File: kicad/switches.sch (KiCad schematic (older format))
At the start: 24 parts, among them SW1 SW_SPDT_MSM, SW2 SW_SPDT_MSM, SW3 SW_SPDT_MSM, SW4 SW_SPDT_MSM, SW5 SW_Push, SW6 SW_Push, SW7 SW_Push, SW8 SW_Push, U1 74LS165, U2 74LS165

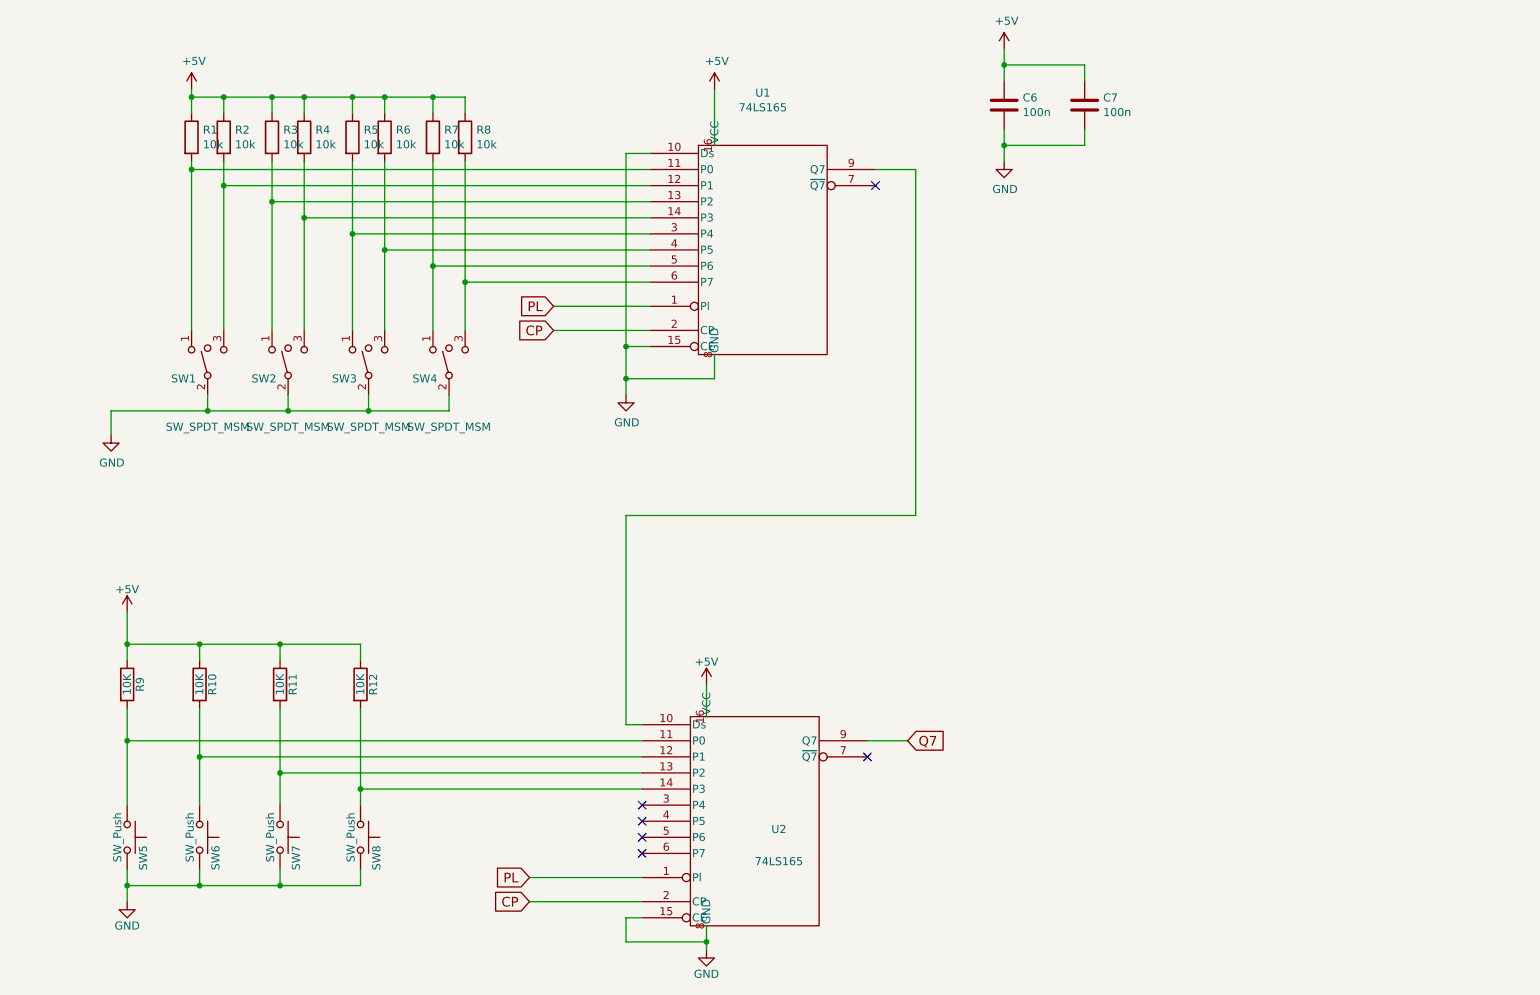
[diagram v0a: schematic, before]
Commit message: Add more switches, footprints.
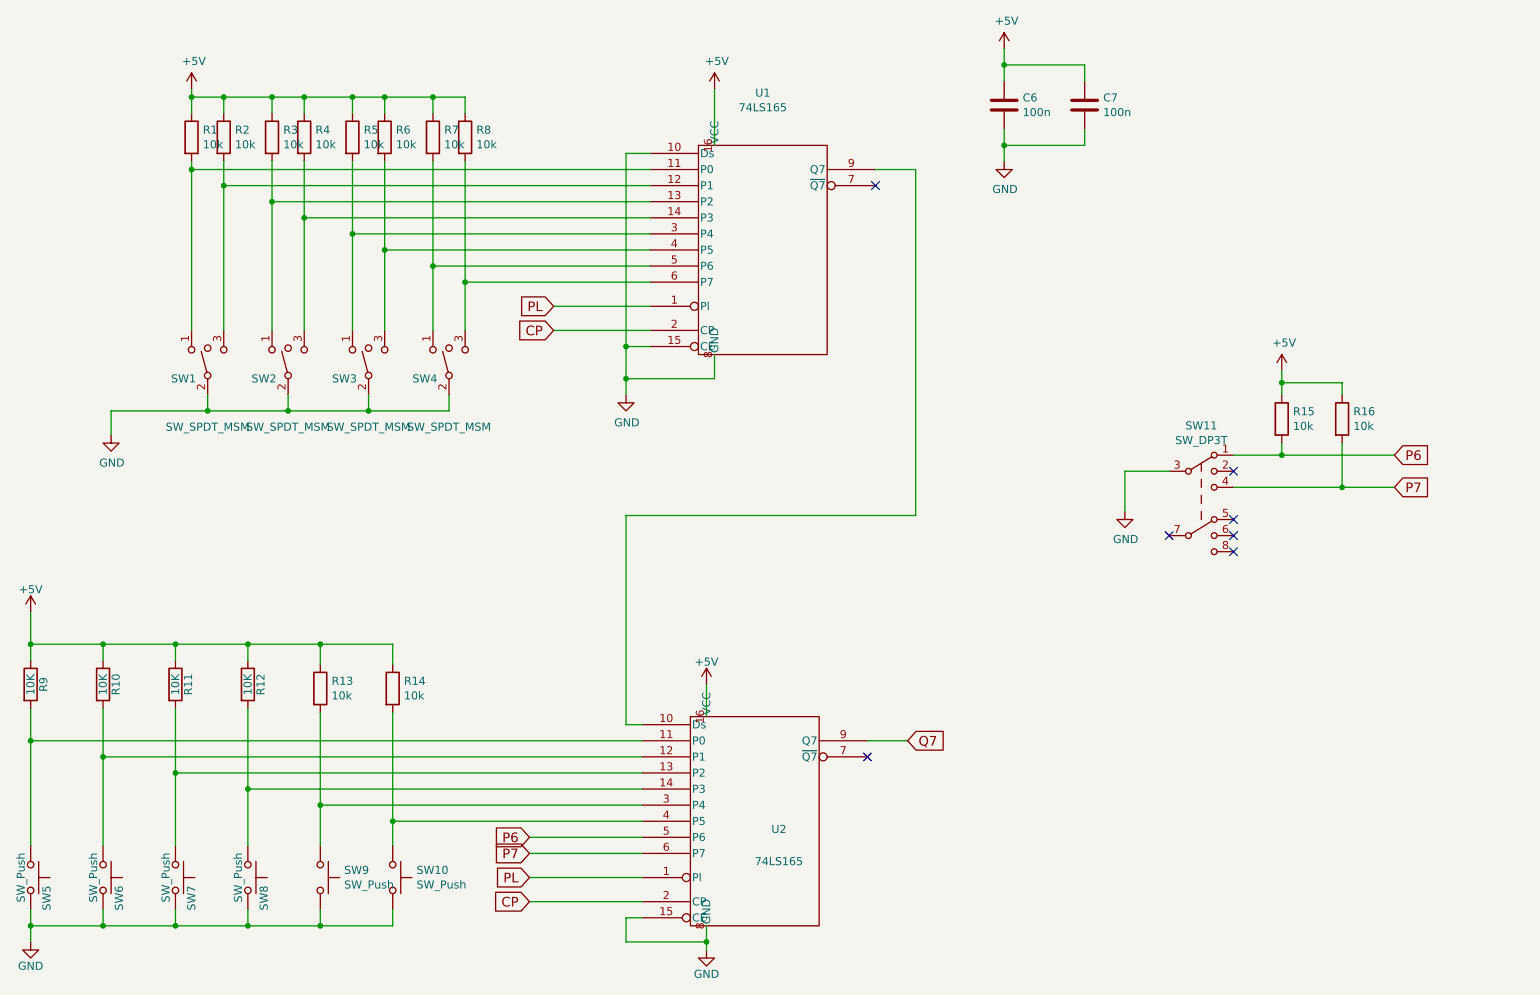
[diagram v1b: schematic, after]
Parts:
- added R13, R14, R15, R16: 10k, Resistor_SMD:R_0805_2012Metric, symbol Device:R
- added SW10, SW9: SW_Push, Remote:Switch_1x02_P6mm, symbol remote-rescue:SW_Push
- added SW11: SW_DP3T, symbol remote:SW_DP3T
- SW5, SW6, SW7, SW8: footprint Remote:Switch_1x02_P8mm -> Remote:Switch_1x02_P6mm
- U1, U2: footprint Package_DIP:DIP-16_W7.62mm_LongPads -> Milling:DIP-16_W7.62mm_Milling
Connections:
- net +5V: now also R13.1, R14.1, R15.1, R16.1
- net GND: now also SW10.2, SW11.3, SW9.2
- net at U2.3 (P4): now also R13.2, SW9.1
- net at U2.4 (P5): now also R14.2, SW10.1
- net P6: now reaches U2.5 (P6)
- net P6: now also R15.2, SW11.1
- net P7: now reaches U2.6 (P7)
- net P7: now also R16.2, SW11.4
- no-connect marks 6 -> 7
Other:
- moved on the sheet: R10, R11, R12, R9, SW5, SW6, SW7, SW8

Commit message: Place switches, etc. Split up into two boards.
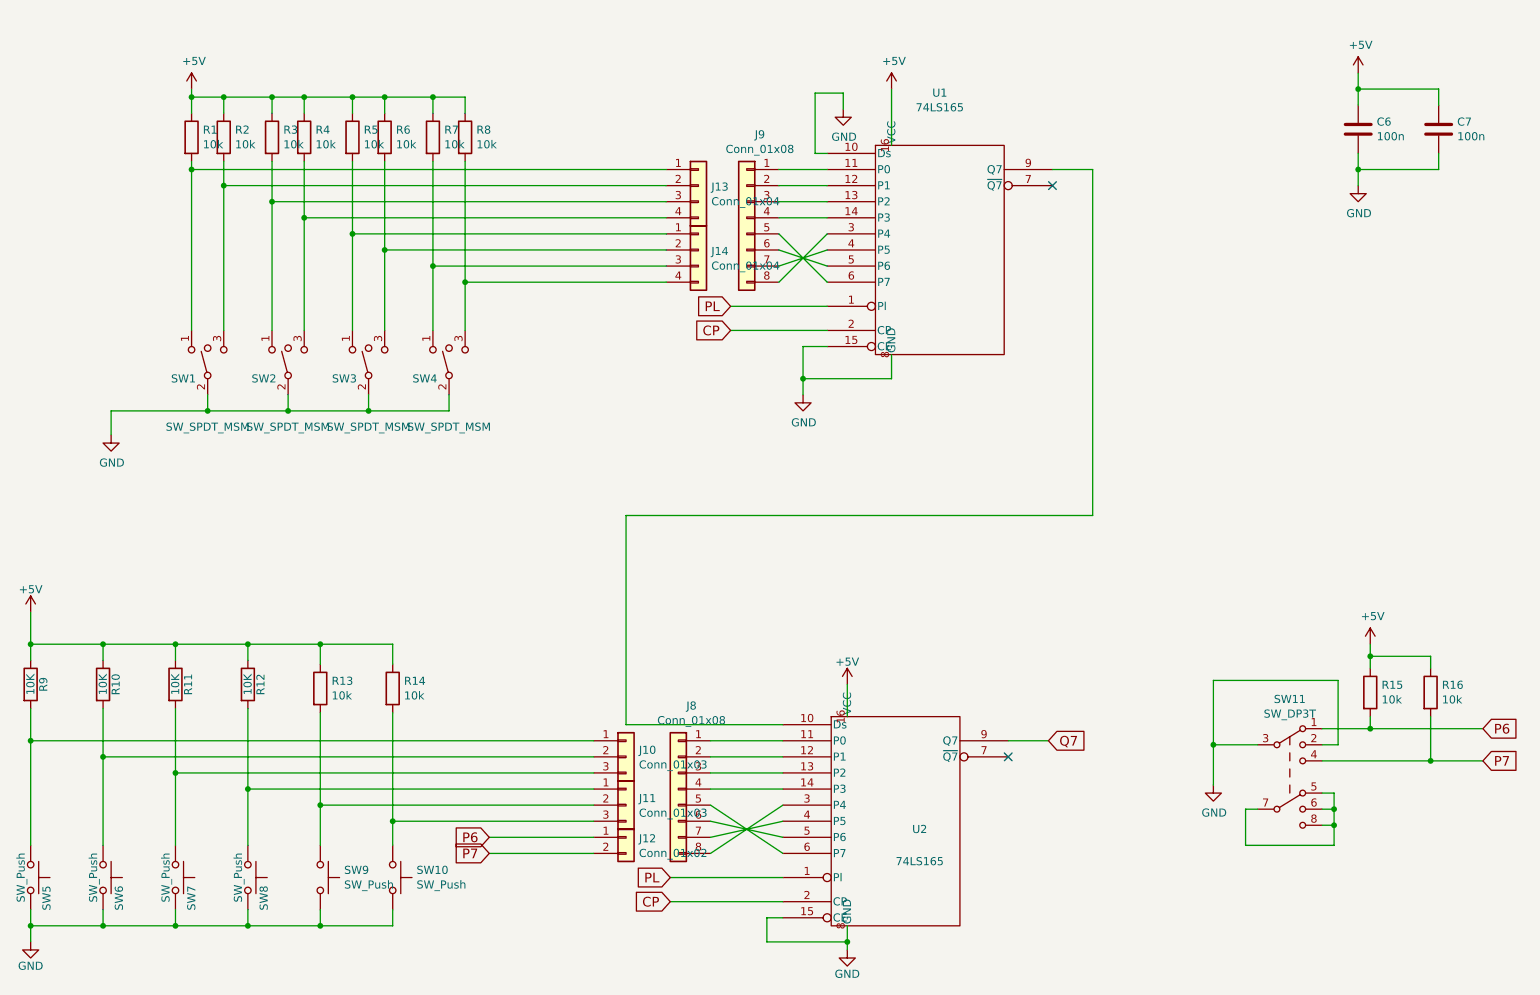
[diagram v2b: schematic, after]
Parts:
- added J10, J11: Conn_01x03, Milling:JST_XH_B03B-XH-A_1x03_P2.50mm_Vertical_Milling, symbol Connector_Generic:Conn_01x03
- added J12: Conn_01x02, Milling:JST_XH_B02B-XH-A_1x02_P2.50mm_Vertical_Milling, symbol Connector_Generic:Conn_01x02
- added J13, J14: Conn_01x04, Milling:JST_XH_B04B-XH-A_1x04_P2.50mm_Vertical_Milling, symbol Connector_Generic:Conn_01x04
- added J8, J9: Conn_01x08, Connector_JST:JST_XH_B08B-XH-A_1x08_P2.50mm_Vertical, symbol Connector_Generic:Conn_01x08
- SW11: footprint (none) -> Remote:Switch_2x03_P3mm_Slide
- U1, U2: footprint Milling:DIP-16_W7.62mm_Milling -> Package_DIP:DIP-16_W7.62mm
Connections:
- net GND: now also SW11.2
- net P6: now also J12.1 (Pin_1); no longer U2.5 (P6)
- net P7: now also J12.2 (Pin_2); no longer U2.6 (P7)
- net at R9.2, SW5.1: now also J10.1 (Pin_1); no longer U2.11 (P0)
- net at R10.2, SW6.1: now also J10.2 (Pin_2); no longer U2.12 (P1)
- net at R11.2, SW7.1: now also J10.3 (Pin_3); no longer U2.13 (P2)
- net at R12.2, SW8.1: now also J11.1 (Pin_1); no longer U2.14 (P3)
- net at R1.2, SW1.1: now also J13.1 (Pin_1); no longer U1.11 (P0)
- net at R2.2, SW1.3: now also J13.2 (Pin_2); no longer U1.12 (P1)
- net at R3.2, SW2.1: now also J13.3 (Pin_3); no longer U1.13 (P2)
- net at R4.2, SW2.3: now also J13.4 (Pin_4); no longer U1.14 (P3)
- net at R5.2, SW3.1: now also J14.1 (Pin_1); no longer U1.3 (P4)
- net at R6.2, SW3.3: now also J14.2 (Pin_2); no longer U1.4 (P5)
- net at R7.2, SW4.1: now also J14.3 (Pin_3); no longer U1.5 (P6)
- net at R8.2, SW4.3: now also J14.4 (Pin_4); no longer U1.6 (P7)
- net at R13.2, SW9.1: now also J11.2 (Pin_2); no longer U2.3 (P4)
- net at R14.2, SW10.1: now also J11.3 (Pin_3); no longer U2.4 (P5)
- net at SW11.5: now also SW11.6, SW11.7, SW11.8
- new net: J8.1 (Pin_1), U2.11 (P0)
- new net: J8.2 (Pin_2), U2.12 (P1)
- new net: J8.3 (Pin_3), U2.13 (P2)
- new net: J8.4 (Pin_4), U2.14 (P3)
- new net: J8.8 (Pin_8), U2.3 (P4)
- new net: J8.7 (Pin_7), U2.4 (P5)
- new net: J8.6 (Pin_6), U2.5 (P6)
- new net: J8.5 (Pin_5), U2.6 (P7)
- new net: J9.1 (Pin_1), U1.11 (P0)
- new net: J9.2 (Pin_2), U1.12 (P1)
- new net: J9.3 (Pin_3), U1.13 (P2)
- new net: J9.4 (Pin_4), U1.14 (P3)
- new net: J9.8 (Pin_8), U1.3 (P4)
- new net: J9.7 (Pin_7), U1.4 (P5)
- new net: J9.6 (Pin_6), U1.5 (P6)
- new net: J9.5 (Pin_5), U1.6 (P7)
- no-connect marks 7 -> 2
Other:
- moved on the sheet: C6, C7, R15, R16, SW11, U1, U2
